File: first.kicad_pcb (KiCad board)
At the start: 2 copper layers, 55 x 100 mm, 48 parts, among them J1 Conn_01x02_Socket, J10 Conn_01x02_Socket, J11 USB_C_Receptacle_USB2.0_16P, J12 Conn_01x03_Socket, J13 Conn_01x02_Socket, J14 Conn_01x02_Socket, J2 Conn_01x03_Socket, J3 Conn_01x03_Socket, J4 Conn_01x03_Socket, J5 Conn_01x03_Socket, J6 Conn_01x03_Socket, J7 Conn_01x03_Socket, J8 Conn_01x03_Socket, J9 Conn_01x03_Socket, SW1 SW_Push, SW3 SW_Wuerth_450301014042, U1 STM32F446RETx, U2 MCP2561-E-SN, U3 CH340E, U4 BD33FC0FP

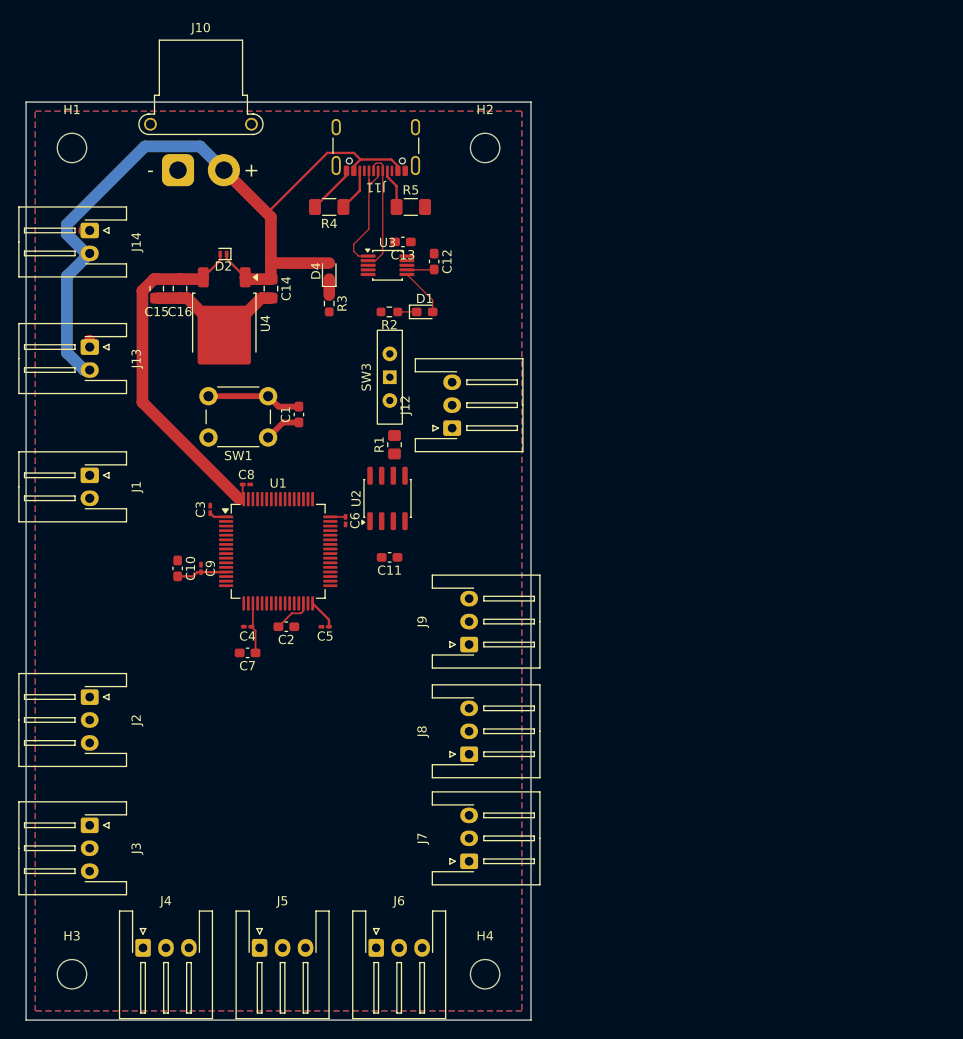
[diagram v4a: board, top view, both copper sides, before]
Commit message: mcpモジュールの変更、stlinkV3の追加
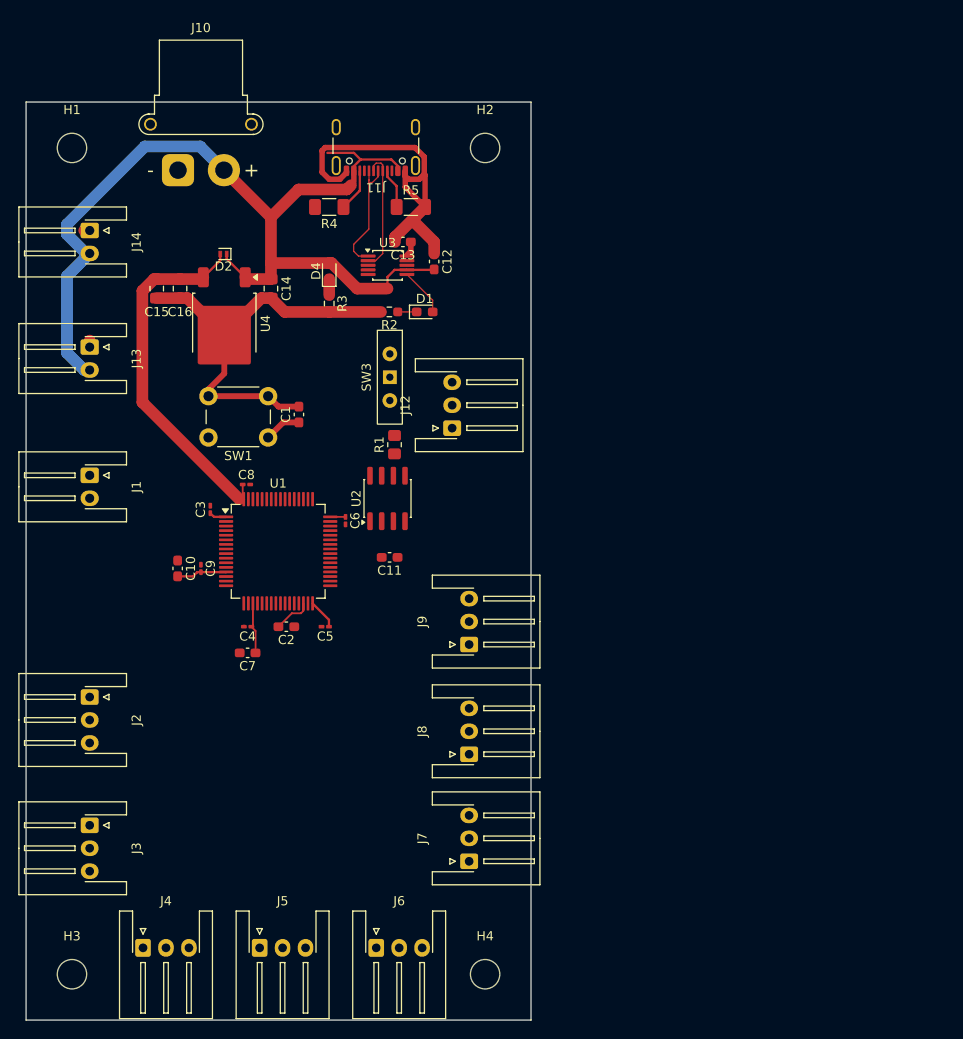
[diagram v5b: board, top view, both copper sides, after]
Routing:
- net GND: track 32.9 -> 88.4 mm
- net +5V: track 90.7 -> 103.2 mm
- net Net-(U3-V3): track 0.00 -> 1.59 mm
- removed copper zone on B.Cu, net GND
- removed copper zone on F.Cu, net GND

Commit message: 回路図の微調整、pcbエディターでの配線、完成版ver1
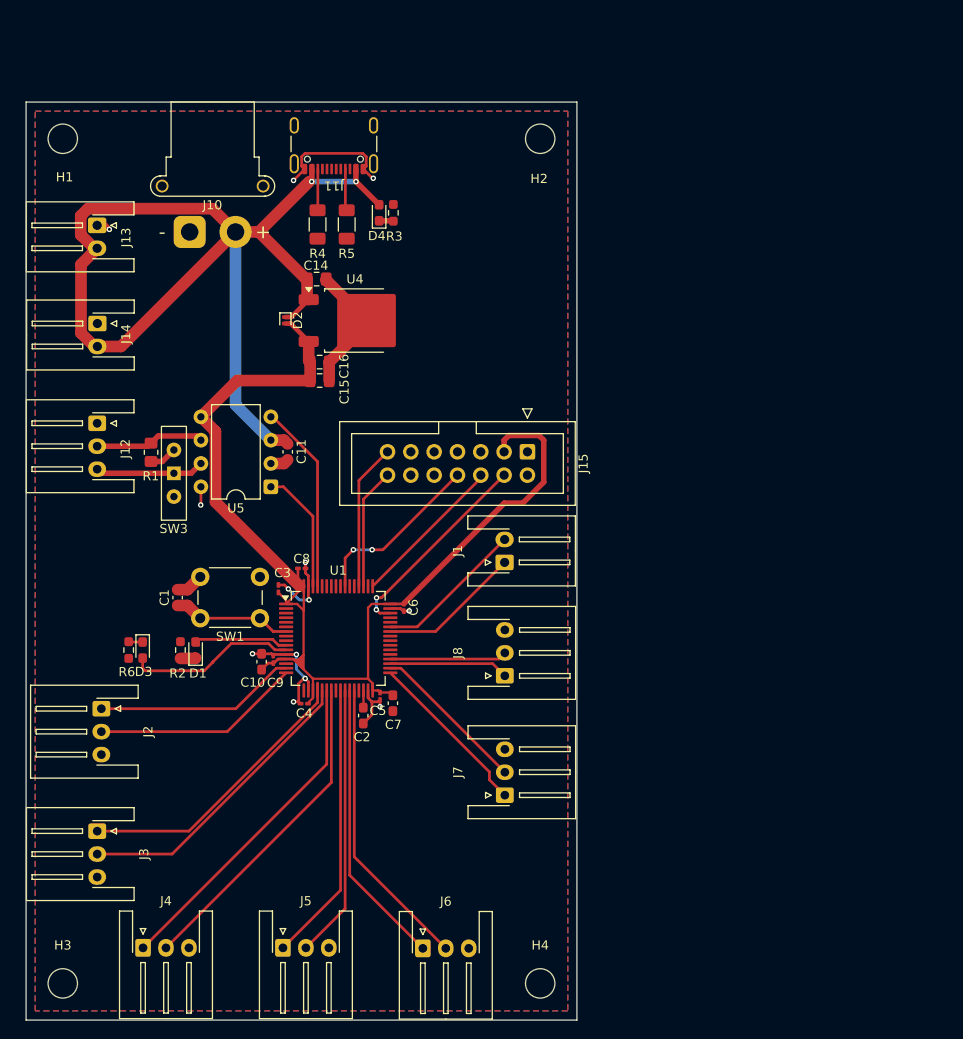
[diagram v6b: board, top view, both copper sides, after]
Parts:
- removed C12, C13: 0.1uf, Capacitor_SMD:C_0603_1608Metric_Pad1.08x0.95mm_HandSolder
- removed J9: Conn_01x03_Socket, Connector_JST:JST_XH_S3B-XH-A-1_1x03_P2.50mm_Horizontal
- removed U2: MCP2561-E-SN, Package_SO:SOIC-8_3.9x4.9mm_P1.27mm
- removed U3: CH340E, Package_SO:MSOP-10_3x3mm_P0.5mm
- added D3: LED_WHITE, Diode_SMD:D_0603_1608Metric_Pad1.05x0.95mm_HandSolder, F.Cu at (62.7, 109.7)
- added J15: Conn_ST_STDC14, Connector_IDC:IDC-Header_2x07_P2.54mm_Vertical, F.Cu at (104.6, 88.1)
- added R6: 120, Resistor_SMD:R_0603_1608Metric_Pad0.98x0.95mm_HandSolder, F.Cu at (61.2, 109.7)
- added U5: MCP2562-E-P, Package_DIP:DIP-8_W7.62mm, F.Cu at (76.7, 91.9)
- R2, R3: value 75 -> 120
- moved J1 46.2 mm to (102.1, 100.1), turned to 90 degrees
- moved D1 44.5 mm to (68.5, 109.7), turned to 90 degrees
- moved R2 43.3 mm to (66.8, 109.7), turned to -90 degrees
- moved J12 38.7 mm to (57.7, 85.0), turned to -90 degrees
- moved R1 26.5 mm to (63.6, 88.2), turned to -90 degrees
- moved SW3 25.7 mm to (66.1, 90.4), turned to 90 degrees
- moved C1 23.9 mm to (66.5, 104.0)
- moved C15 20.4 mm to (82.0, 80.3), turned to 0 degrees
- moved SW1 19.7 mm to (75.5, 106.2)
- moved C16 17.2 mm to (82.0, 78.3), turned to 0 degrees
- moved C7 16.7 mm to (90.0, 115.5), turned to -90 degrees
- moved C11 16.0 mm to (78.5, 88.1), turned to -90 degrees
- moved U4 14.2 mm to (85.8, 73.8), turned to 0 degrees
- moved C10 13.7 mm to (75.7, 111.0)
- moved J13 13.3 mm to (57.7, 63.4)
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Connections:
- J11 pad A6: D+ -> unconnected-(J11-D+-PadA6)
- J11 pad A7: D- -> unconnected-(J11-D--PadA7)
- J11 pad B6: D+ -> unconnected-(J11-D+-PadB6)
- J11 pad B7: D- -> unconnected-(J11-D--PadB7)
- J12 pad 1: CAN_L -> GND
- J12 pad 2: GND -> CAN_L
- R2 pad 1: Net-(D1-K) -> GND
- R2 pad 2: GND -> Net-(D1-K)
- U1 pad 10: m8d -> Net-(D1-A)
- U1 pad 11: unconnected-(U1-PC3-Pad11) -> Net-(D3-A)
- U1 pad 14: uart4tx -> unconnected-(U1-PA0-Pad14)
- U1 pad 15: uart4rx -> m1d
- U1 pad 16: UARTtx -> m1
- U1 pad 17: UARTrx -> unconnected-(U1-PA3-Pad17)
- U1 pad 2: m1d -> unconnected-(U1-PC13-Pad2)
- U1 pad 20: unconnected-(U1-PA4-Pad20) -> m2d
- U1 pad 21: m1 -> m2
- U1 pad 22: m2 -> m3d
- U1 pad 23: unconnected-(U1-PA7-Pad23) -> m3
- U1 pad 25: unconnected-(U1-PC5-Pad25) -> m4d
- U1 pad 26: m8 -> m4
- U1 pad 27: m7 -> m5d
- U1 pad 28: unconnected-(U1-PB2-Pad28) -> m5
- U1 pad 29: m5 -> unconnected-(U1-PB10-Pad29)
- U1 pad 3: m2d -> unconnected-(U1-PC14-Pad3)
- U1 pad 33: unconnected-(U1-PB12-Pad33) -> m6d
- U1 pad 34: unconnected-(U1-PB13-Pad34) -> m6
- U1 pad 35: unconnected-(U1-PB14-Pad35) -> m7d
- U1 pad 36: unconnected-(U1-PB15-Pad36) -> m7
- U1 pad 4: m3d -> unconnected-(U1-PC15-Pad4)
- U1 pad 42: unconnected-(U1-PA9-Pad42) -> uart4tx
- U1 pad 43: m6 -> uart4rx
- U1 pad 44: CAN1rx -> unconnected-(U1-PA11-Pad44)
- U1 pad 45: CAN1tx -> unconnected-(U1-PA12-Pad45)
- U1 pad 46: m4d -> swdio
- U1 pad 49: m5d -> swclk
- U1 pad 50: m6d -> unconnected-(U1-PA15-Pad50)
- U1 pad 51: unconnected-(U1-PC10-Pad51) -> sttx
- U1 pad 52: unconnected-(U1-PC11-Pad52) -> strx
- U1 pad 55: m3 -> swo
- U1 pad 57: m4 -> unconnected-(U1-PB5-Pad57)
- U1 pad 59: m7d -> unconnected-(U1-PB7-Pad59)
- U1 pad 61: unconnected-(U1-PB8-Pad61) -> CAN1rx
- U1 pad 62: unconnected-(U1-PB9-Pad62) -> CAN1tx
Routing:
- net +3.3V: track 57.2 -> 129.1 mm
- net m3d: track 0.00 -> 36.3 mm
- net m3: track 0.00 -> 35.5 mm
- net m2: track 0.00 -> 32.7 mm
- net m5: track 0.00 -> 32.2 mm
- net m2d: track 0.00 -> 31.9 mm
- net m5d: track 0.00 -> 31.4 mm
- net m4d: track 0.00 -> 30.6 mm
- net m4: track 0.00 -> 29.8 mm
- net m1: track 0.00 -> 22.8 mm
- net swdio: track 0.00 -> 22.4 mm, vias 0 -> 2
- net m1d: track 0.00 -> 22.0 mm
- net GND: track 88.4 -> 66.4 mm, vias 0 -> 13
- net CAN1rx: track 0.00 -> 20.7 mm
- net swo: track 0.00 -> 19.1 mm, vias 0 -> 2
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- added copper zone on B.Cu, net GND
- added copper zone on F.Cu, net GND
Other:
- board size 55 x 100 mm -> 60 x 100 mm

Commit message: PCBAの仕様に沿った部品に変更、再配置
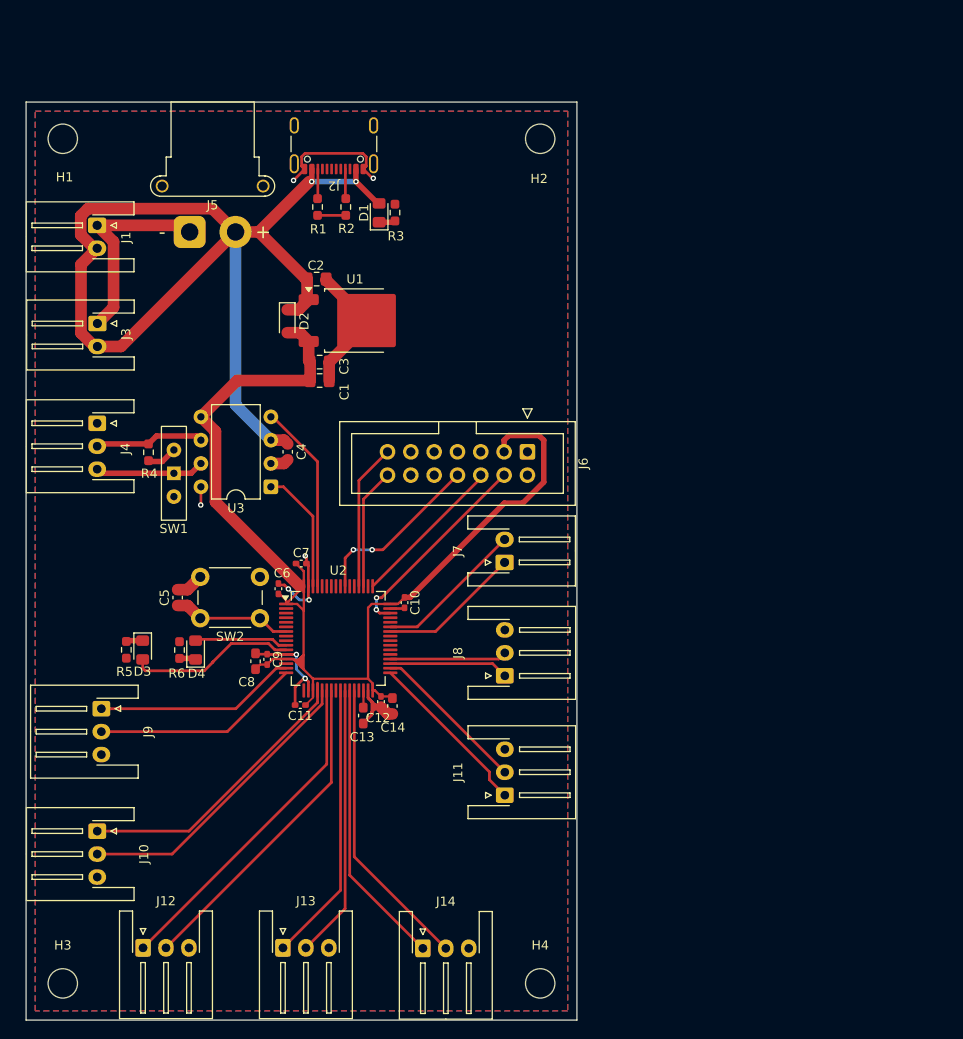
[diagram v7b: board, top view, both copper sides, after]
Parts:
- C10: renamed from C6; value 0.1μF -> 0.1uF; footprint Capacitor_SMD:C_0201_0603Metric_Pad0.64x0.40mm_HandSolder -> Capacitor_SMD:C_0402_1005Metric_Pad0.74x0.62mm_HandSolder
- C11: renamed from C4; value 0.1μF -> 0.1uF; footprint Capacitor_SMD:C_0201_0603Metric_Pad0.64x0.40mm_HandSolder -> Capacitor_SMD:C_0402_1005Metric_Pad0.74x0.62mm_HandSolder
- C12: renamed from C5; value 0.1μF -> 0.1uF; footprint Capacitor_SMD:C_0201_0603Metric_Pad0.64x0.40mm_HandSolder -> Capacitor_SMD:C_0402_1005Metric_Pad0.74x0.62mm_HandSolder
- C6: renamed from C3; value 0.1μF -> 0.1uF; footprint Capacitor_SMD:C_0201_0603Metric_Pad0.64x0.40mm_HandSolder -> Capacitor_SMD:C_0402_1005Metric_Pad0.74x0.62mm_HandSolder
- C7: renamed from C8; value 0.1μF -> 0.1uF; footprint Capacitor_SMD:C_0201_0603Metric_Pad0.64x0.40mm_HandSolder -> Capacitor_SMD:C_0402_1005Metric_Pad0.74x0.62mm_HandSolder
- C9: footprint Capacitor_SMD:C_0201_0603Metric_Pad0.64x0.40mm_HandSolder -> Capacitor_SMD:C_0402_1005Metric_Pad0.74x0.62mm_HandSolder
- D1: renamed from D4; footprint Diode_SMD:D_0603_1608Metric_Pad1.05x0.95mm_HandSolder -> Diode_SMD:D_0805_2012Metric_Pad1.15x1.40mm_HandSolder
- D2: footprint Diode_SMD:D_SOD-882 -> Diode_SMD:D_SOD-323_HandSoldering
- D3: value LED_WHITE -> LED_YELLOW; footprint Diode_SMD:D_0603_1608Metric_Pad1.05x0.95mm_HandSolder -> Diode_SMD:D_0805_2012Metric_Pad1.15x1.40mm_HandSolder
- D4: renamed from D1; footprint Diode_SMD:D_0603_1608Metric_Pad1.05x0.95mm_HandSolder -> Diode_SMD:D_0805_2012Metric_Pad1.15x1.40mm_HandSolder
- R1: renamed from R4; footprint Resistor_SMD:R_1206_3216Metric_Pad1.30x1.75mm_HandSolder -> Resistor_SMD:R_0603_1608Metric_Pad0.98x0.95mm_HandSolder
- R2: renamed from R5; footprint Resistor_SMD:R_1206_3216Metric_Pad1.30x1.75mm_HandSolder -> Resistor_SMD:R_0603_1608Metric_Pad0.98x0.95mm_HandSolder
- R4: renamed from R1; footprint Resistor_SMD:R_0805_2012Metric_Pad1.20x1.40mm_HandSolder -> Resistor_SMD:R_0603_1608Metric_Pad0.98x0.95mm_HandSolder
- moved R2 1.91 mm to (84.8, 61.4)
- moved R1 1.91 mm to (81.8, 61.4)
- moved C8 0.66 mm to (75.0, 110.9)
- moved C9 0.66 mm to (76.3, 110.7)
- moved C12 0.60 mm to (88.7, 115.3)
- moved C7 0.54 mm to (80.0, 100.3)
- moved C10 0.52 mm to (91.2, 104.5)
- moved C11 0.46 mm to (79.9, 115.7)
- moved C14 0.31 mm to (89.9, 115.8)
- moved R4 0.28 mm to (63.3, 88.2)
- moved R5 0.26 mm to (60.9, 109.7)
- moved D2 0.23 mm to (78.4, 73.9)
- moved R3 0.18 mm to (90.2, 62.0)
- moved R6 0.10 mm to (66.7, 109.7)
- renumbered C15 to C1, C2 to C13, C7 to C14, C14 to C2, C16 to C3, C11 to C4, C1 to C5, C10 to C8, J13 to J1, J3 to J10, J7 to J11, J4 to J12, J5 to J13, J6 to J14, J11 to J2, J14 to J3, J12 to J4, J10 to J5, J15 to J6, J1 to J7, J2 to J9, R6 to R5, R2 to R6, SW3 to SW1, SW1 to SW2, U4 to U1, U1 to U2, U5 to U3
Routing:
- net GND: track 66.4 -> 93.0 mm, vias 13 -> 8
- net Net-(J11-CC1): track 4.55 -> 3.24 mm
- net Net-(J11-CC2): track 4.50 -> 3.23 mm
- net +3.3V: track 129.1 -> 130.1 mm
- net +5V: track 116.0 -> 115.4 mm
- net Net-(D1-A): track 10.7 -> 10.2 mm

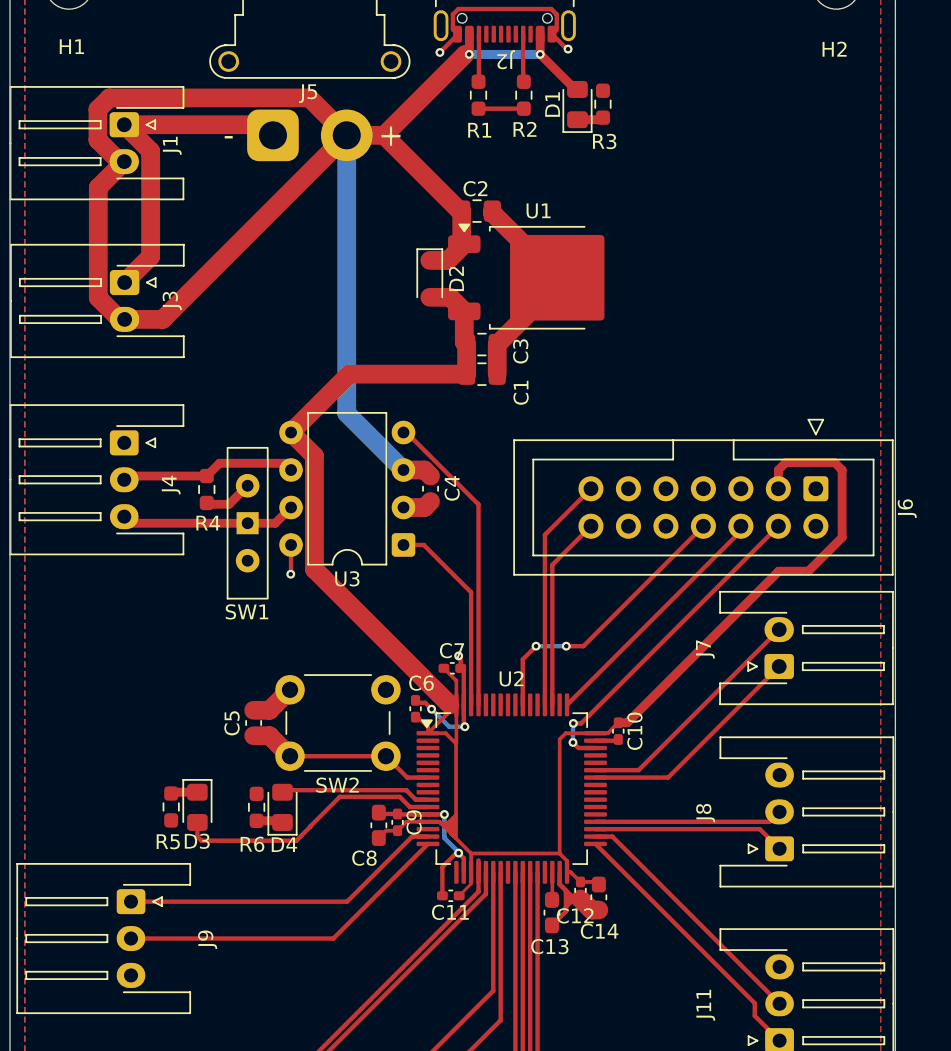
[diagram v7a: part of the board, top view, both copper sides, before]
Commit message: stdc14のコネクタをきちんとしたものに取り換え、5V供給端子のループを解消
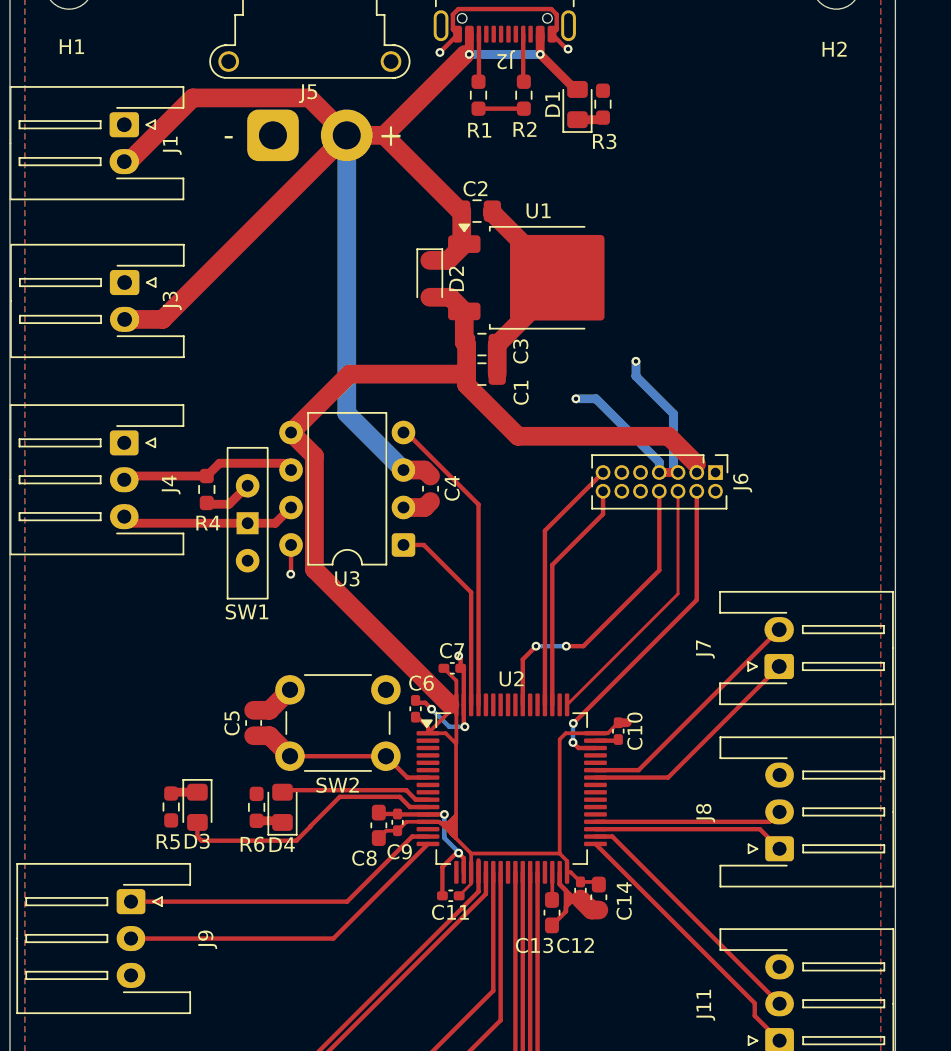
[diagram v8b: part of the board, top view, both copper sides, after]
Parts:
- J6: footprint Connector_IDC:IDC-Header_2x07_P2.54mm_Vertical -> Connector_PinHeader_1.27mm:PinHeader_2x07_P1.27mm_Vertical
- moved J6 6.89 mm to (97.8, 87.0)
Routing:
- net +5V: track 115.4 -> 98.9 mm
- net +3.3V: track 130.1 -> 118.3 mm
- net GND: track 93.0 -> 90.0 mm, vias 8 -> 10
- net sttx: track 13.2 -> 15.9 mm
- net strx: track 15.9 -> 17.4 mm
- net swo: track 19.1 -> 20.2 mm
- net swclk: track 17.0 -> 17.6 mm
